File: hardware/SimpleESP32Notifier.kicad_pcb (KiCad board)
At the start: 2 copper layers, 60 x 70 mm, 13 parts, among them SW1 SW_Push, SW2 SW_Push, SW3 SW_Push, U1 Heltec_HTIT-WB32

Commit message: Rounded corners
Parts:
- R1, R2, R3: value 10k -> 10kΩ
- R4, R5, R6: value 220 -> 220Ω
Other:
- outline, holes or cut-outs redrawn

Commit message: Finished schematic
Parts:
- R1, R2, R3: value 10kΩ -> 10k
- R4, R5, R6: value 220Ω -> 220
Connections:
- U1 pad 11: unconnected-(U1-3.3-Pad11) -> +3.3V
- U1 pad 28: unconnected-(U1-GND-Pad28) -> GND
- U1 pad 8: unconnected-(U1-GND-Pad8) -> GND
- U1 pad 9: unconnected-(U1-3.3-Pad9) -> +3.3V

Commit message: Exported V1.0
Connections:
- U1 pad 11: +3.3V -> unconnected-(U1-3.3-Pad11)
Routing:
- net +3.3V: track 0.00 -> 56.1 mm
- net BUT_1: track 0.00 -> 48.2 mm
- net BUT_2: track 0.00 -> 43.1 mm
- net BUT_3: track 0.00 -> 38.0 mm
- net LED_1: track 0.00 -> 17.9 mm
- net LED_2: track 0.00 -> 12.8 mm
- net LED_3: track 0.00 -> 8.30 mm
- net Net-(D3-A): track 0.00 -> 8.08 mm
- net Net-(D1-A): track 0.00 -> 7.93 mm
- net Net-(D2-A): track 0.00 -> 7.93 mm
- added copper zone on B.Cu, net GND
- added copper zone on F.Cu, net GND

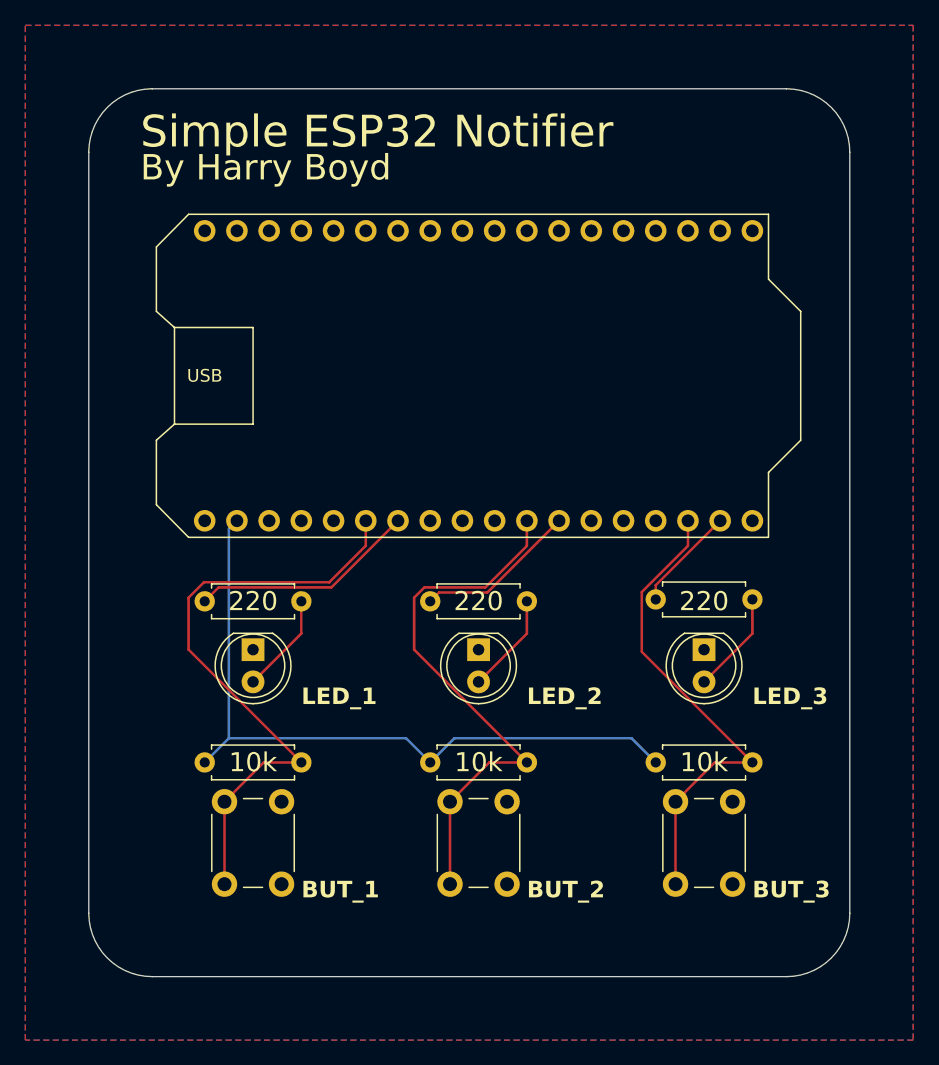
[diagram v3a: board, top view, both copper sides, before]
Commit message: Fixed pins wiring of v1.0
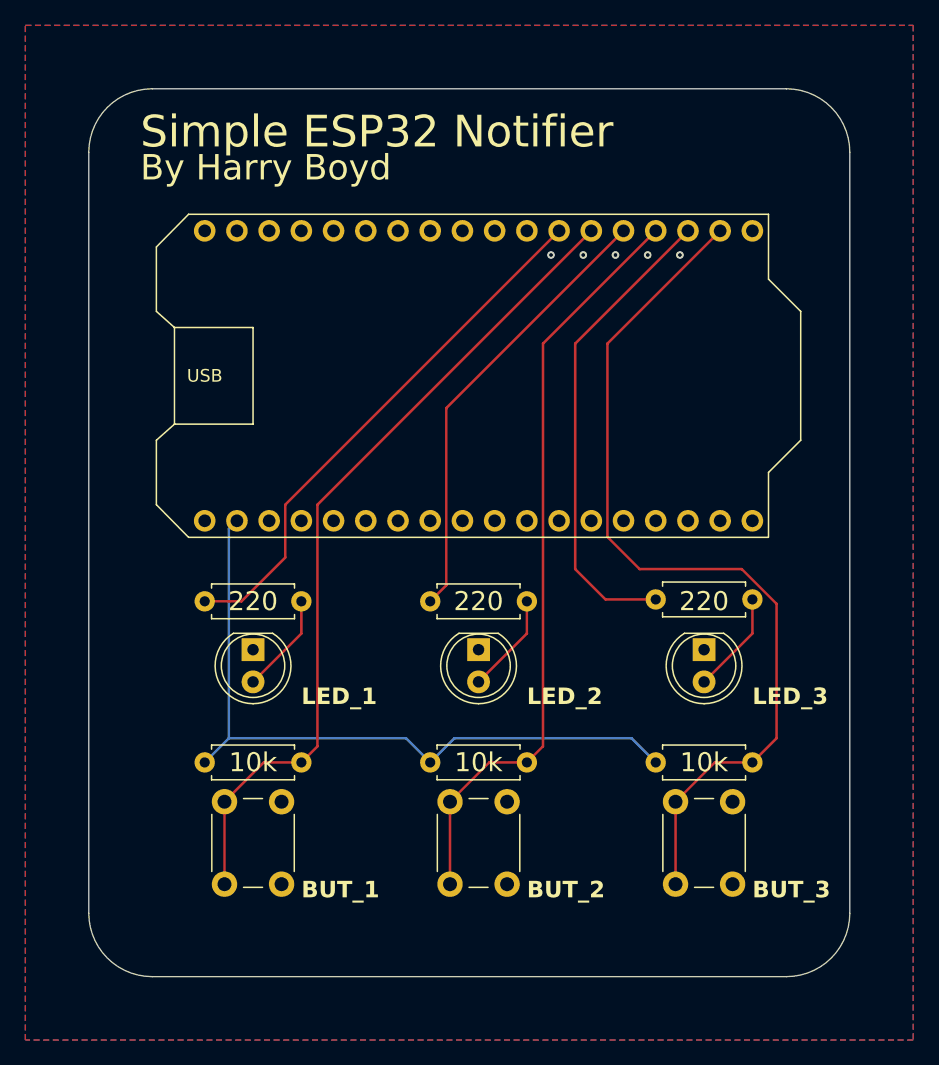
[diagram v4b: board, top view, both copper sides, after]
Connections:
- U1 pad 12: BUT_1 -> unconnected-(U1-Pad12)
- U1 pad 14: LED_1 -> unconnected-(U1-Pad14)
- U1 pad 17: unconnected-(U1-Pad17) -> LED_1
- U1 pad 18: unconnected-(U1-Pad18) -> LED_2
- U1 pad 19: unconnected-(U1-Pad19) -> LED_3
- U1 pad 22: unconnected-(U1-Pad22) -> BUT_3
- U1 pad 23: unconnected-(U1-Pad23) -> BUT_2
- U1 pad 32: LED_2 -> unconnected-(U1-Pad32)
- U1 pad 33: BUT_2 -> unconnected-(U1-Pad33)
- U1 pad 37: LED_3 -> unconnected-(U1-Pad37)
- U1 pad 38: BUT_3 -> unconnected-(U1-Pad38)
- U1 pad 5: unconnected-(U1-Pad5) -> BUT_1
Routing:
- net BUT_3: track 38.0 -> 70.5 mm
- net LED_3: track 8.30 -> 37.7 mm
- net LED_1: track 17.9 -> 42.5 mm
- net LED_2: track 12.8 -> 35.5 mm
- net BUT_1: track 48.2 -> 65.2 mm
- net BUT_2: track 43.1 -> 60.0 mm
- net GND: vias 0 -> 5
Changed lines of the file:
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@@
 	(net 2 "unconnected-(U1-4_OLED-Pad4)")
 	(net 3 "unconnected-(U1-Pad27)")
-	(net 4 "unconnected-(U1-Pad18)")
+	(net 4 "unconnected-(U1-Pad38)")
 	(net 5 "unconnected-(U1-16_OLED-Pad16)")
-	(net 6 "unconnected-(U1-Pad22)")
-	(net 7 "unconnected-(U1-Pad19)")
+	(net 6 "unconnected-(U1-Pad37)")
+	(net 7 "unconnected-(U1-Pad32)")
 	(net 8 "unconnected-(U1-Pad21)")
 	(net 9 "unconnected-(U1-5V-Pad20)")
@@
 	(net 11 "unconnected-(U1-TX-Pad1)")
 	(net 12 "unconnected-(U1-Pad34)")
-	(net 13 "unconnected-(U1-Pad23)")
+	(net 13 "unconnected-(U1-Pad14)")
 	(net 14 "unconnected-(U1-Pad39)")
 	(net 15 "unconnected-(U1-Pad13)")
@@
 	(net 17 "unconnected-(U1-Vext-Pad7)")
 	(net 18 "unconnected-(U1-Pad35)")
-	(net 19 "unconnected-(U1-Pad17)")
+	(net 19 "unconnected-(U1-Pad33)")
 	(net 20 "unconnected-(U1-25_DAC-Pad25)")
 	(net 21 "unconnected-(U1-Pad0)")
@@
 	(net 25 "unconnected-(U1-15_OLED-Pad15)")
 	(net 26 "unconnected-(U1-Pad2)")
-	(net 27 "unconnected-(U1-Pad5)")
+	(net 27 "unconnected-(U1-Pad12)")
 	(net 28 "Net-(D1-A)")
 	(net 29 "Net-(D2-A)")
@@
 			(layers "*.Cu" "*.Mask")
 			(remove_unused_layers no)
-			(net 27 "unconnected-(U1-Pad5)")
+			(net 35 "BUT_1")
 			(pinfunction "5")
-			(pintype "bidirectional+no_connect")
+			(pintype "bidirectional")
 		)
 		(pad "6" thru_hole circle
@@
 			(layers "*.Cu" "*.Mask")
 			(remove_unused_layers no)
-			(net 35 "BUT_1")
+			(net 27 "unconnected-(U1-Pad12)")
 			(pinfunction "12")
-			(pintype "bidirectional")
+			(pintype "bidirectional+no_connect")
 		)
 		(pad "13" thru_hole circle
@@
 			(layers "*.Cu" "*.Mask")
 			(remove_unused_layers no)
-			(net 33 "LED_1")
+			(net 13 "unconnected-(U1-Pad14)")
 			(pinfunction "14")
-			(pintype "bidirectional")
+			(pintype "bidirectional+no_connect")
 		)
 		(pad "15" thru_hole circle
@@
 			(layers "*.Cu" "*.Mask")
 			(remove_unused_layers no)
-			(net 19 "unconnected-(U1-Pad17)")
+			(net 33 "LED_1")
 			(pinfunction "17")
-			(pintype "bidirectional+no_connect")
+			(pintype "bidirectional")
 		)
 		(pad "18" thru_hole circle
@@
 			(layers "*.Cu" "*.Mask")
 			(remove_unused_layers no)
-			(net 4 "unconnected-(U1-Pad18)")
+			(net 37 "LED_2")
 			(pinfunction "18")
-			(pintype "bidirectional+no_connect")
+			(pintype "bidirectional")
 		)
 		(pad "19" thru_hole circle
@@
 			(layers "*.Cu" "*.Mask")
 			(remove_unused_layers no)
-			(net 7 "unconnected-(U1-Pad19)")
+			(net 38 "LED_3")
 			(pinfunction "19")
-			(pintype "bidirectional+no_connect")
+			(pintype "bidirectional")
 		)
 		(pad "20" thru_hole circle
@@
 			(layers "*.Cu" "*.Mask")
 			(remove_unused_layers no)
-			(net 6 "unconnected-(U1-Pad22)")
+			(net 32 "BUT_3")
 			(pinfunction "22")
-			(pintype "bidirectional+no_connect")
+			(pintype "bidirectional")
 		)
 		(pad "23" thru_hole circle
@@
 			(layers "*.Cu" "*.Mask")
 			(remove_unused_layers no)
-			(net 13 "unconnected-(U1-Pad23)")
+			(net 31 "BUT_2")
 			(pinfunction "23")
-			(pintype "bidirectional+no_connect")
+			(pintype "bidirectional")
 		)
 		(pad "25" thru_hole circle
@@
 			(layers "*.Cu" "*.Mask")
 			(remove_unused_layers no)
-			(net 37 "LED_2")
+			(net 7 "unconnected-(U1-Pad32)")
 			(pinfunction "32")
-			(pintype "input")
+			(pintype "input+no_connect")
 		)
 		(pad "33" thru_hole circle
@@
 			(layers "*.Cu" "*.Mask")
 			(remove_unused_layers no)
-			(net 31 "BUT_2")
+			(net 19 "unconnected-(U1-Pad33)")
 			(pinfunction "33")
-			(pintype "input")
+			(pintype "input+no_connect")
 		)
 		(pad "34" thru_hole circle
@@
 			(layers "*.Cu" "*.Mask")
 			(remove_unused_layers no)
-			(net 38 "LED_3")
+			(net 6 "unconnected-(U1-Pad37)")
 			(pinfunction "37")
-			(pintype "input")
+			(pintype "input+no_connect")
 		)
 		(pad "38" thru_hole circle
@@
 			(layers "*.Cu" "*.Mask")
 			(remove_unused_layers no)
-			(net 32 "BUT_3")
+			(net 4 "unconnected-(U1-Pad38)")
 			(pinfunction "38")
-			(pintype "input")
+			(pintype "input+no_connect")
 		)
 		(pad "39" thru_hole circle
@@
 	)
 	(segment
-		(start 120.65 109.22)
-		(end 129.54 118.11)
-		(width 0.2)
-		(layer "F.Cu")
-		(net 31)
-	)
-	(segment
 		(start 123.48 121.21)
 		(end 126.58 118.11)
@@
 	)
 	(segment
-		(start 121.464365 104.31)
-		(end 120.65 105.124365)
-		(width 0.2)
-		(layer "F.Cu")
-		(net 31)
-	)
-	(segment
-		(start 129.54 101.034314)
-		(end 126.264314 104.31)
+		(start 129.54 118.11)
+		(end 130.81 116.84)
 		(width 0.2)
 		(layer "F.Cu")
@@
 	)
 	(segment
-		(start 120.65 105.124365)
-		(end 120.65 109.22)
+		(start 130.81 85.09)
+		(end 139.7 76.2)
 		(width 0.2)
 		(layer "F.Cu")
@@
 	)
 	(segment
-		(start 126.264314 104.31)
-		(end 121.464365 104.31)
+		(start 130.81 116.84)
+		(end 130.81 85.09)
 		(width 0.2)
 		(layer "F.Cu")
@@
 	)
 	(segment
-		(start 129.54 99.06)
-		(end 129.54 101.034314)
+		(start 146.485635 102.87)
+		(end 138.43 102.87)
 		(width 0.2)
 		(layer "F.Cu")
-		(net 31)
+		(net 32)
 	)
 	(segment
@@
 	)
 	(segment
-		(start 138.6 109.39)
-		(end 147.32 118.11)
+		(start 138.43 102.87)
+		(end 135.89 100.33)
 		(width 0.2)
 		(layer "F.Cu")
@@
 	)
 	(segment
-		(start 142.24 99.06)
-		(end 142.24 101.034314)
+		(start 135.89 100.33)
+		(end 135.89 85.09)
 		(width 0.2)
 		(layer "F.Cu")
@@
 	)
 	(segment
-		(start 142.24 101.034314)
-		(end 138.6 104.674314)
+		(start 135.89 85.09)
+		(end 144.78 76.2)
 		(width 0.2)
 		(layer "F.Cu")
@@
 	)
 	(segment
-		(start 138.6 104.674314)
-		(end 138.6 109.39)
+		(start 147.32 118.11)
+		(end 149.225 116.205)
+		(width 0.2)
+		(layer "F.Cu")
+		(net 32)
+	)
+	(segment
+		(start 149.225 116.205)
+		(end 149.225 105.609365)
 		(width 0.2)
 		(layer "F.Cu")
@@
 	)
 	(segment
+		(start 149.225 105.609365)
+		(end 146.485635 102.87)
+		(width 0.2)
+		(layer "F.Cu")
+		(net 32)
+	)
+	(segment
 		(start 144.36 118.11)
 		(end 147.32 118.11)
@@
 	)
 	(segment
-		(start 105.24 104.31)
-		(end 114.13 104.31)
+		(start 110.49 97.79)
+		(end 132.08 76.2)
 		(width 0.2)
 		(layer "F.Cu")
@@
 	)
 	(segment
-		(start 114.13 104.31)
-		(end 119.38 99.06)
+		(start 107.036346 105.41)
+		(end 110.49 101.956346)
 		(width 0.2)
 		(layer "F.Cu")
@@
 	(segment
 		(start 104.14 105.41)
-		(end 105.24 104.31)
+		(end 107.036346 105.41)
+		(width 0.2)
+		(layer "F.Cu")
+		(net 33)
+	)
+	(segment
+		(start 110.49 101.956346)
+		(end 110.49 97.79)
 		(width 0.2)
 		(layer "F.Cu")
@@
 	)
 	(segment
-		(start 116.84 99.06)
-		(end 116.84 101.034314)
+		(start 108.8 118.11)
+		(end 111.76 118.11)
 		(width 0.2)
 		(layer "F.Cu")
@@
 	)
 	(segment
-		(start 108.8 118.11)
-		(end 111.76 118.11)
+		(start 113.03 116.84)
+		(end 113.03 97.79)
 		(width 0.2)
 		(layer "F.Cu")
@@
 	)
 	(segment
-		(start 102.87 109.22)
-		(end 111.76 118.11)
+		(start 105.7 121.21)
+		(end 108.8 118.11)
 		(width 0.2)
 		(layer "F.Cu")
@@
 	)
 	(segment
-		(start 102.87 105.124365)
-		(end 102.87 109.22)
+		(start 111.76 118.11)
+		(end 113.03 116.84)
 		(width 0.2)
 		(layer "F.Cu")
@@
 	)
 	(segment
-		(start 113.964314 103.91)
-		(end 104.084365 103.91)
+		(start 113.03 97.79)
+		(end 134.62 76.2)
 		(width 0.2)
 		(layer "F.Cu")
 		(net 35)
 	)
-	(segment
-		(start 105.7 121.21)
-		(end 108.8 118.11)
-		(width 0.2)
-		(layer "F.Cu")
-		(net 35)
+	(via
+		(at 141.605 78.105)
+		(size 0.6)
+		(drill 0.3)
+		(layers "F.Cu" "B.Cu")
+		(free yes)
+		(net 36)
+	)
+	(via
+		(at 136.525 78.105)
+		(size 0.6)
+		(drill 0.3)
+		(layers "F.Cu" "B.Cu")
+		(free yes)
+		(net 36)
+	)
+	(via
+		(at 133.985 78.105)
+		(size 0.6)
+		(drill 0.3)
+		(layers "F.Cu" "B.Cu")
+		(free yes)
+		(net 36)
+	)
+	(via
+		(at 139.065 78.105)
+		(size 0.6)
+		(drill 0.3)
+		(layers "F.Cu" "B.Cu")
+		(free yes)
+		(net 36)
+	)
+	(via
+		(at 131.445 78.105)
+		(size 0.6)
+		(drill 0.3)
+		(layers "F.Cu" "B.Cu")
+		(free yes)
+		(net 36)
 	)
 	(segment
-		(start 104.084365 103.91)
-		(end 102.87 105.124365)
+		(start 121.92 105.41)
+		(end 123.19 104.14)
 		(width 0.2)
 		(layer "F.Cu")
-		(net 35)
+		(net 37)
 	)
 	(segment
-		(start 116.84 101.034314)
-		(end 113.964314 103.91)
+		(start 123.19 90.17)
+		(end 137.16 76.2)
 		(width 0.2)
 		(layer "F.Cu")
-		(net 35)
+		(net 37)
 	)
 	(segment
-		(start 126.43 104.71)
-		(end 132.08 99.06)
+		(start 123.19 104.14)
+		(end 123.19 90.17)
 		(width 0.2)
 		(layer "F.Cu")
@@
 	)
 	(segment
-		(start 121.92 105.41)
-		(end 122.62 104.71)
+		(start 135.74 105.26)
+		(end 133.35 102.87)
 		(width 0.2)
 		(layer "F.Cu")
-		(net 37)
+		(net 38)
 	)
 	(segment
-		(start 122.62 104.71)
-		(end 126.43 104.71)
+		(start 133.35 102.87)
+		(end 133.35 85.09)
 		(width 0.2)
 		(layer "F.Cu")
-		(net 37)
+		(net 38)
 	)
 	(segment
 		(start 139.7 105.26)
-		(end 139.7 104.14)
+		(end 135.74 105.26)
 		(width 0.2)
 		(layer "F.Cu")
@@
 	)
 	(segment
-		(start 139.7 104.14)
-		(end 144.78 99.06)
+		(start 133.35 85.09)
+		(end 142.24 76.2)
 		(width 0.2)
 		(layer "F.Cu")
